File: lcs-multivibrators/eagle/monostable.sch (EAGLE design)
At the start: 9 parts, among them T1 BC547, T2 BC547

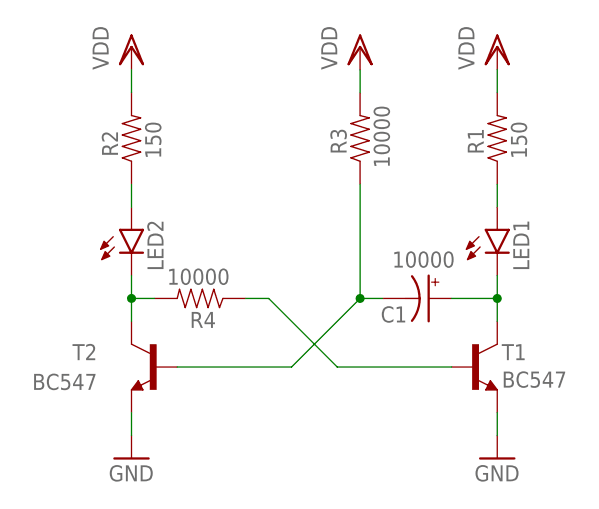
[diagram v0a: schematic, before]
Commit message: multivibrators: fix a few mistakes found during presentation
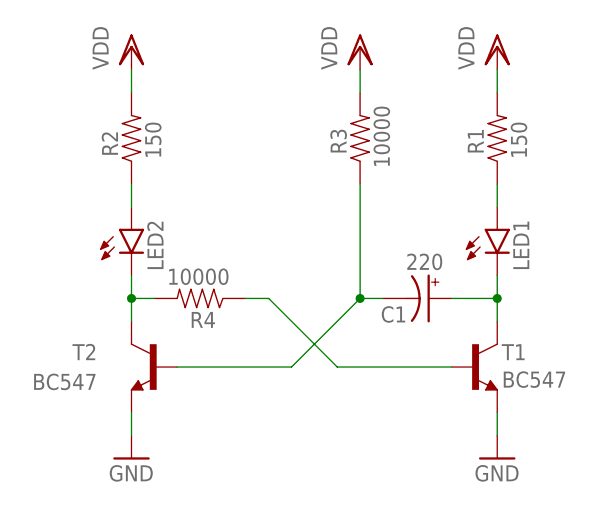
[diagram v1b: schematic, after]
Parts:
- C1: value 10000 -> 220
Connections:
- net N$6: now also C1.-
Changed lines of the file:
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@@
 <part name="R4" library="SparkFun-Passives" deviceset="RESISTOR" device="PTH-1/2W" value="10000"/>
 <part name="VDD3" library="supply1" deviceset="VDD" device=""/>
-<part name="C1" library="SparkFun-Passives" deviceset="CAP_POL" device="PTH4" value="10000"/>
+<part name="C1" library="SparkFun-Passives" deviceset="CAP_POL" device="PTH4" value="220"/>
 </parts>
 <sheets>
@@
 <instance part="C1" gate="G$1" x="27.94" y="60.96" smashed="yes" rot="R270">
 <attribute name="NAME" x="22.606" y="58.293" size="1.778" layer="95"/>
-<attribute name="VALUE" x="23.876" y="64.389" size="1.778" layer="96"/>
+<attribute name="VALUE" x="25.4" y="64.135" size="1.778" layer="96"/>
 </instance>
 </instances>
@@
 <wire x1="20.32" y1="60.96" x2="22.86" y2="60.96" width="0.1524" layer="91"/>
 <junction x="20.32" y="60.96"/>
+<pinref part="C1" gate="G$1" pin="-"/>
 </segment>
 </net>
